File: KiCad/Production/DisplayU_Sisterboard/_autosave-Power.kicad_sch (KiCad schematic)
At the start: 16 parts, among them Q2 AO3421E, U3 AP2112K-3.3TRG1

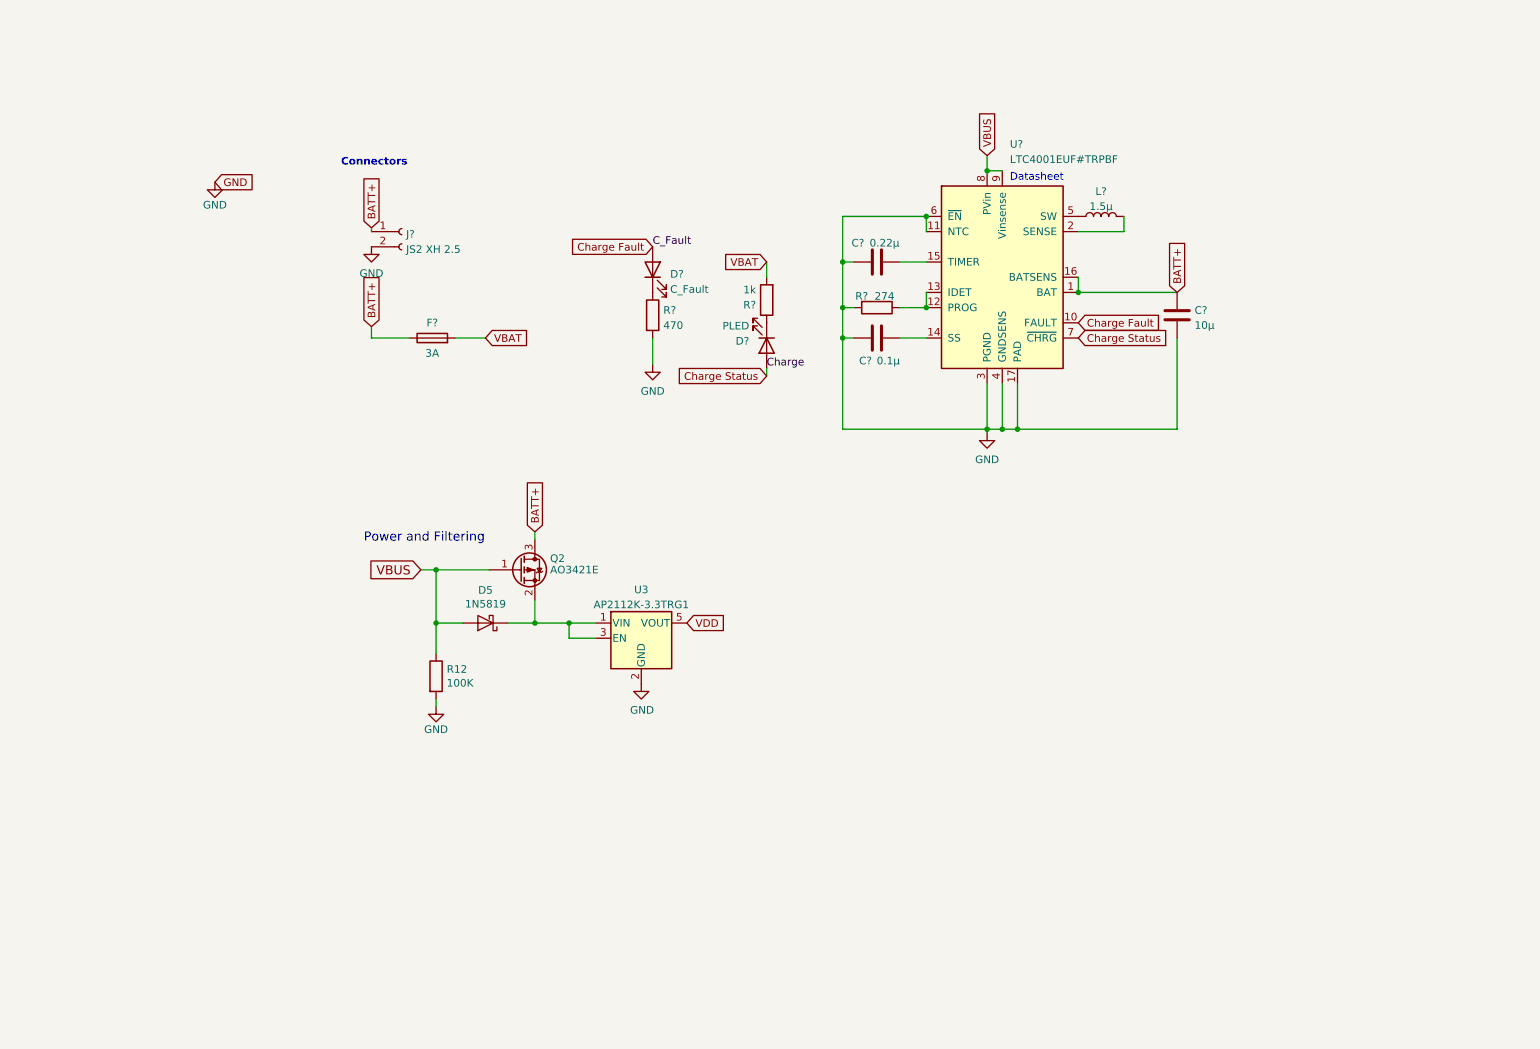
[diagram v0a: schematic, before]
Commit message: added fpga pins
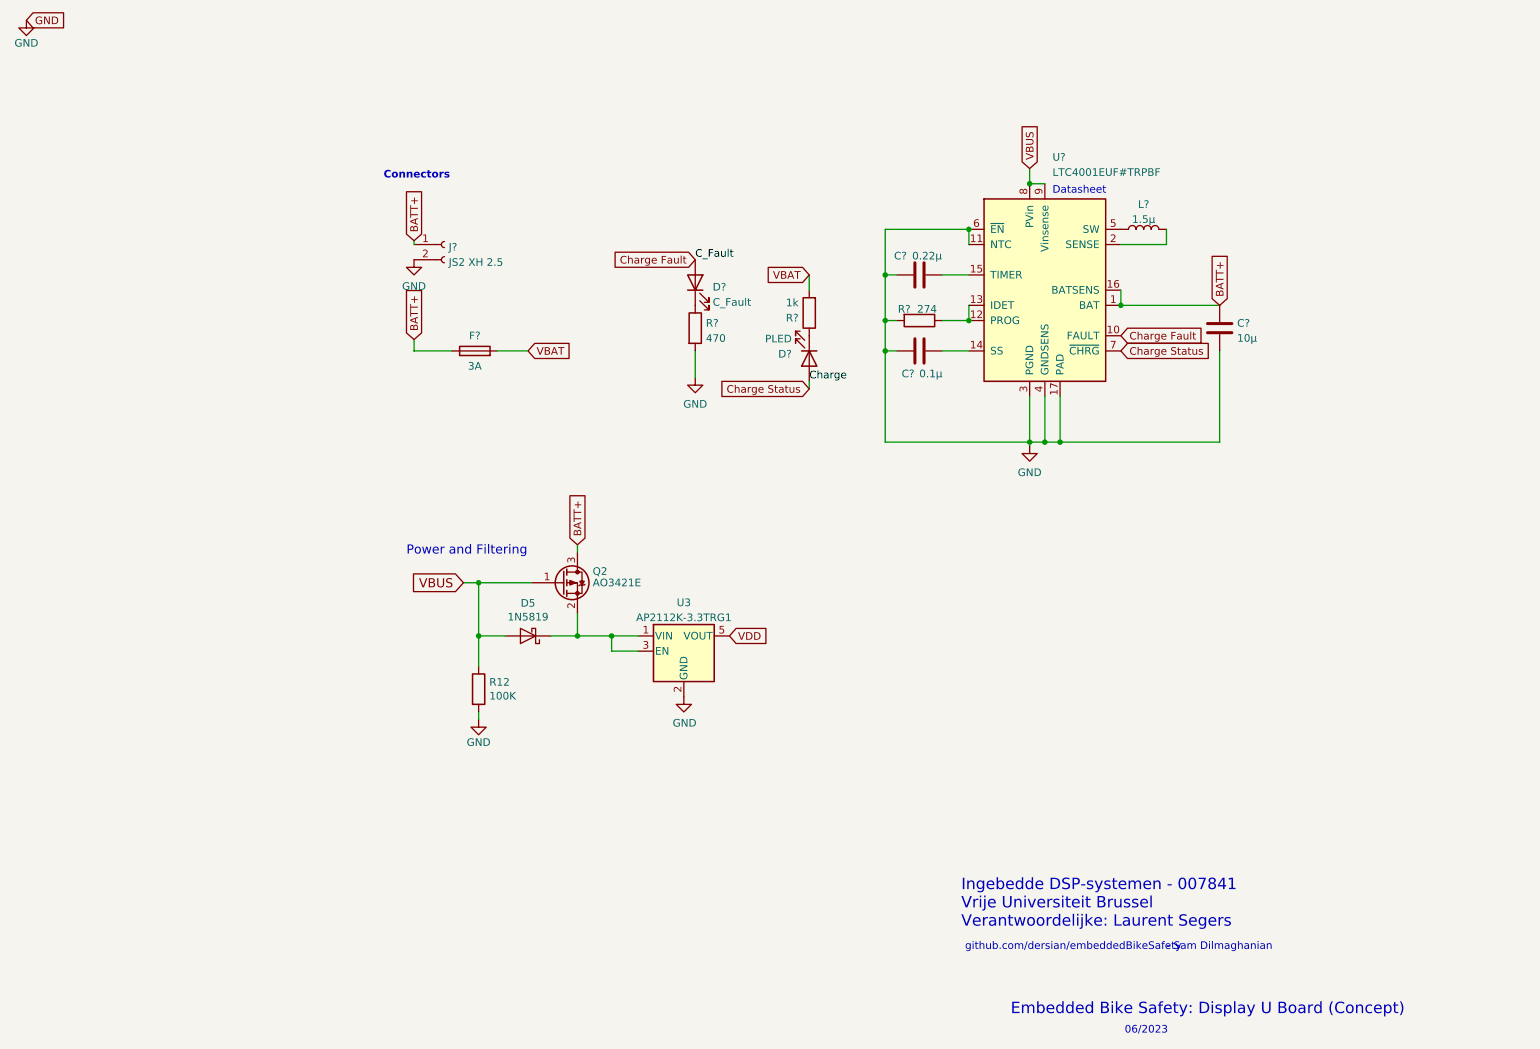
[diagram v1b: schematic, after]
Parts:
- removed C?: 0.22µ, Capacitor_SMD:C_0603_1608Metric_Pad1.08x0.95mm_HandSolder, symbol Device:C
- removed C?: 10µ, Capacitor_SMD:C_0603_1608Metric_Pad1.08x0.95mm_HandSolder, symbol Device:C
- removed C?: 0.1µ, Capacitor_SMD:C_0603_1608Metric_Pad1.08x0.95mm_HandSolder, symbol Device:C
- removed D?: PLED, LED_SMD:LED_0603_1608Metric, symbol Device:LED
- removed D?: C_Fault, LED_SMD:LED_0603_1608Metric, symbol Device:LED
- removed F?: 3A, Fuse:Fuse_0603_1608Metric, symbol Device:Fuse
- removed J?: JS2 XH 2.5, Connector_JST:JST_PH_S2B-PH-SM4-TB_1x02-1MP_P2.00mm_Horizontal, symbol Connector:Conn_01x02_Female
- removed L?: 1.5µ, Inductor_SMD:L_1210_3225Metric, symbol Device:L
- removed R?: 470, Resistor_SMD:R_0603_1608Metric, symbol Device:R
- removed R?: 274, Resistor_SMD:R_0603_1608Metric, symbol Device:R
- removed R?: 1k, Resistor_SMD:R_0603_1608Metric, symbol Device:R
- removed U?: LTC4001EUF#TRPBF, Package_DFN_QFN:QFN-16-1EP_4x4mm_P0.65mm_EP2.15x2.15mm, symbol Battery_Management:LTC4001
- added C?: 0.1µ, Capacitor_SMD:C_0603_1608Metric_Pad1.08x0.95mm_HandSolder, symbol Device:C
- added C?: 0.22µ, Capacitor_SMD:C_0603_1608Metric_Pad1.08x0.95mm_HandSolder, symbol Device:C
- added C?: 10µ, Capacitor_SMD:C_0603_1608Metric_Pad1.08x0.95mm_HandSolder, symbol Device:C
- added D?: C_Fault, LED_SMD:LED_0603_1608Metric, symbol Device:LED
- added D?: PLED, LED_SMD:LED_0603_1608Metric, symbol Device:LED
- added F?: 3A, Fuse:Fuse_0603_1608Metric, symbol Device:Fuse
- added J?: JS2 XH 2.5, Connector_JST:JST_PH_S2B-PH-SM4-TB_1x02-1MP_P2.00mm_Horizontal, symbol Connector:Conn_01x02_Female
- added L?: 1.5µ, Inductor_SMD:L_1210_3225Metric, symbol Device:L
- added R?: 274, Resistor_SMD:R_0603_1608Metric, symbol Device:R
- added R?: 1k, Resistor_SMD:R_0603_1608Metric, symbol Device:R
- added R?: 470, Resistor_SMD:R_0603_1608Metric, symbol Device:R
- added U?: LTC4001EUF#TRPBF, Package_DFN_QFN:QFN-16-1EP_4x4mm_P0.65mm_EP2.15x2.15mm, symbol Battery_Management:LTC4001
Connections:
- net BATT+: now also C?.1, F?.1, J?.1 (Pin_1), U?.1 (BAT), U?.16 (BATSENS)
- net Charge Fault: now also D?.2 (A), U?.10 (FAULT)
- net Charge Status: now also D?.2 (A), U?.7 (~{CHRG})
- net GND: now also C?.1, C?.1, C?.2, J?.2 (Pin_2), R?.2, R?.2, U?.11 (NTC), U?.17 (PAD), U?.3 (PGND), U?.4 (GNDSENS), U?.6 (~{EN})
- net VBAT: now also F?.2, R?.2
- net VBUS: now also U?.8 (PVin), U?.9 (Vinsense)
- new net: C?.2, U?.14 (SS)
- new net: R?.1, U?.12 (PROG), U?.13 (IDET)
- new net: C?.2, U?.15 (TIMER)
- new net: L?.2, U?.2 (SENSE)
- new net: L?.1, U?.5 (SW)
- new net: D?.1 (K), R?.1 (x2)
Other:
- note added: "- Sam Dilmaghanian"
- note added: "06/2023"
- note added: "Embedded Bike Safety: Display U Board (Concept)"
- note added: "Ingebedde DSP-systemen - 007841 Vrije Universiteit Brussel Verantwoordelijke: Laurent Segers"
- note added: "github.com/dersian/embeddedBikeSafety"
